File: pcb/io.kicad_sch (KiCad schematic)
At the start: 36 parts, among them J10 Conn_01x02, J2 RJ18, J3 RJ18, J4 Conn_02x05, J5 Conn_01x03, J6 Conn_01x03, J7 Conn_01x02, J8 Conn_01x02, J9 Conn_01x02, Q1 BT148, Q2 BC847, Q3 BC847, U7 6N137, U8 PC817, U9 PC817

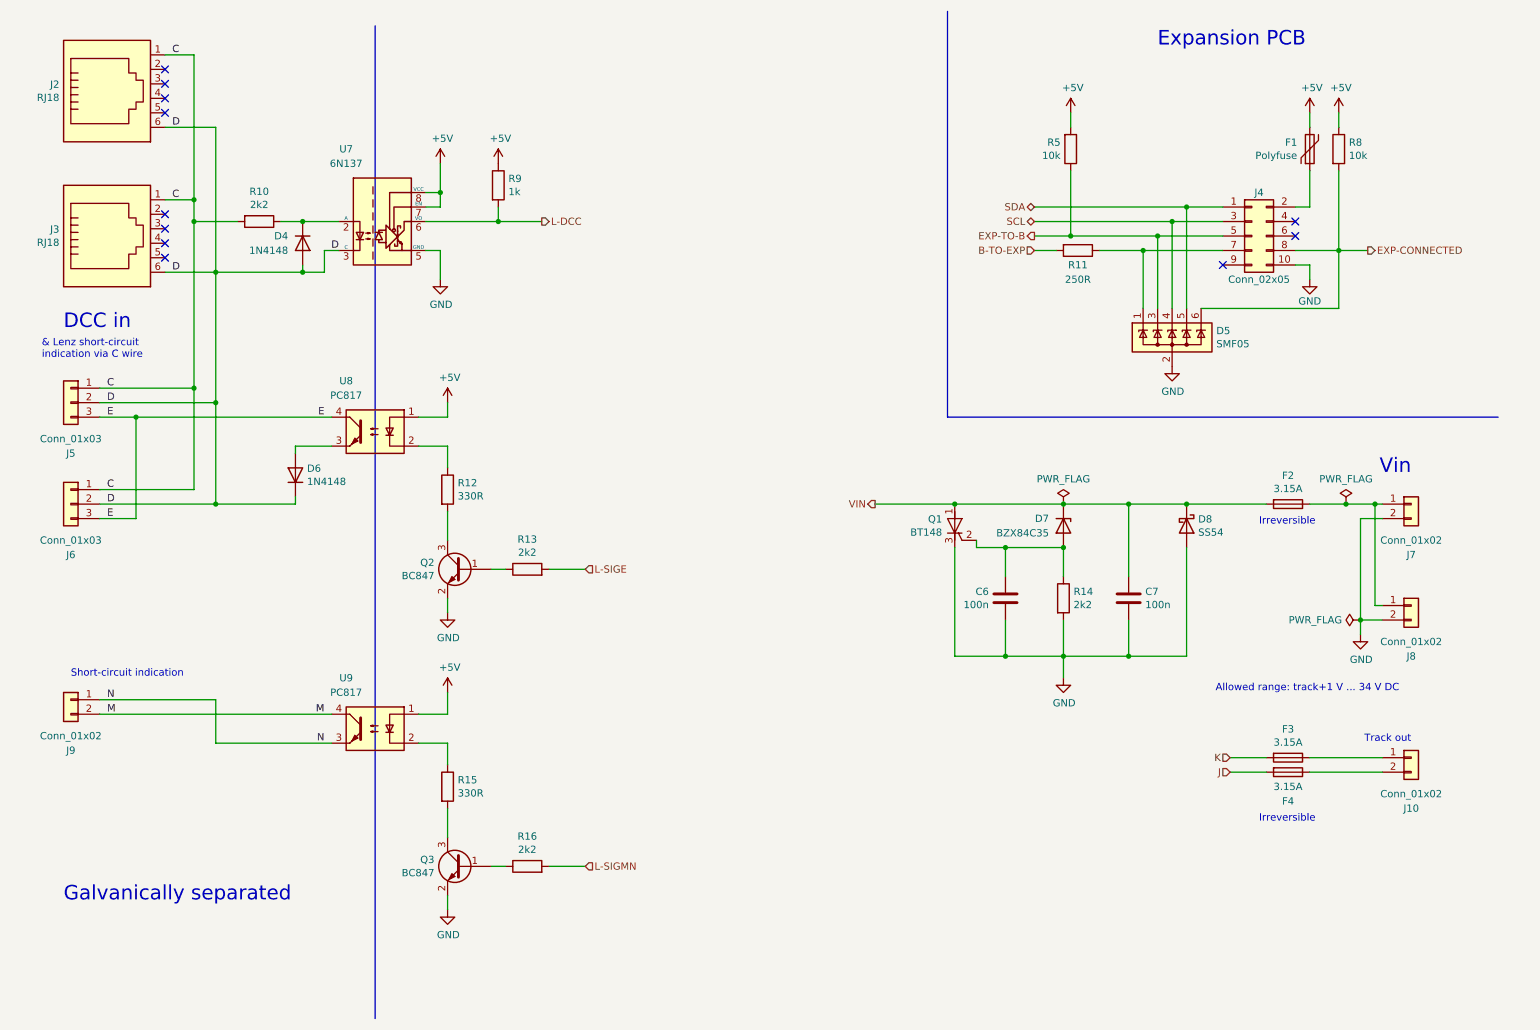
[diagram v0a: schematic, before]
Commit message: Update to KiCad 8.
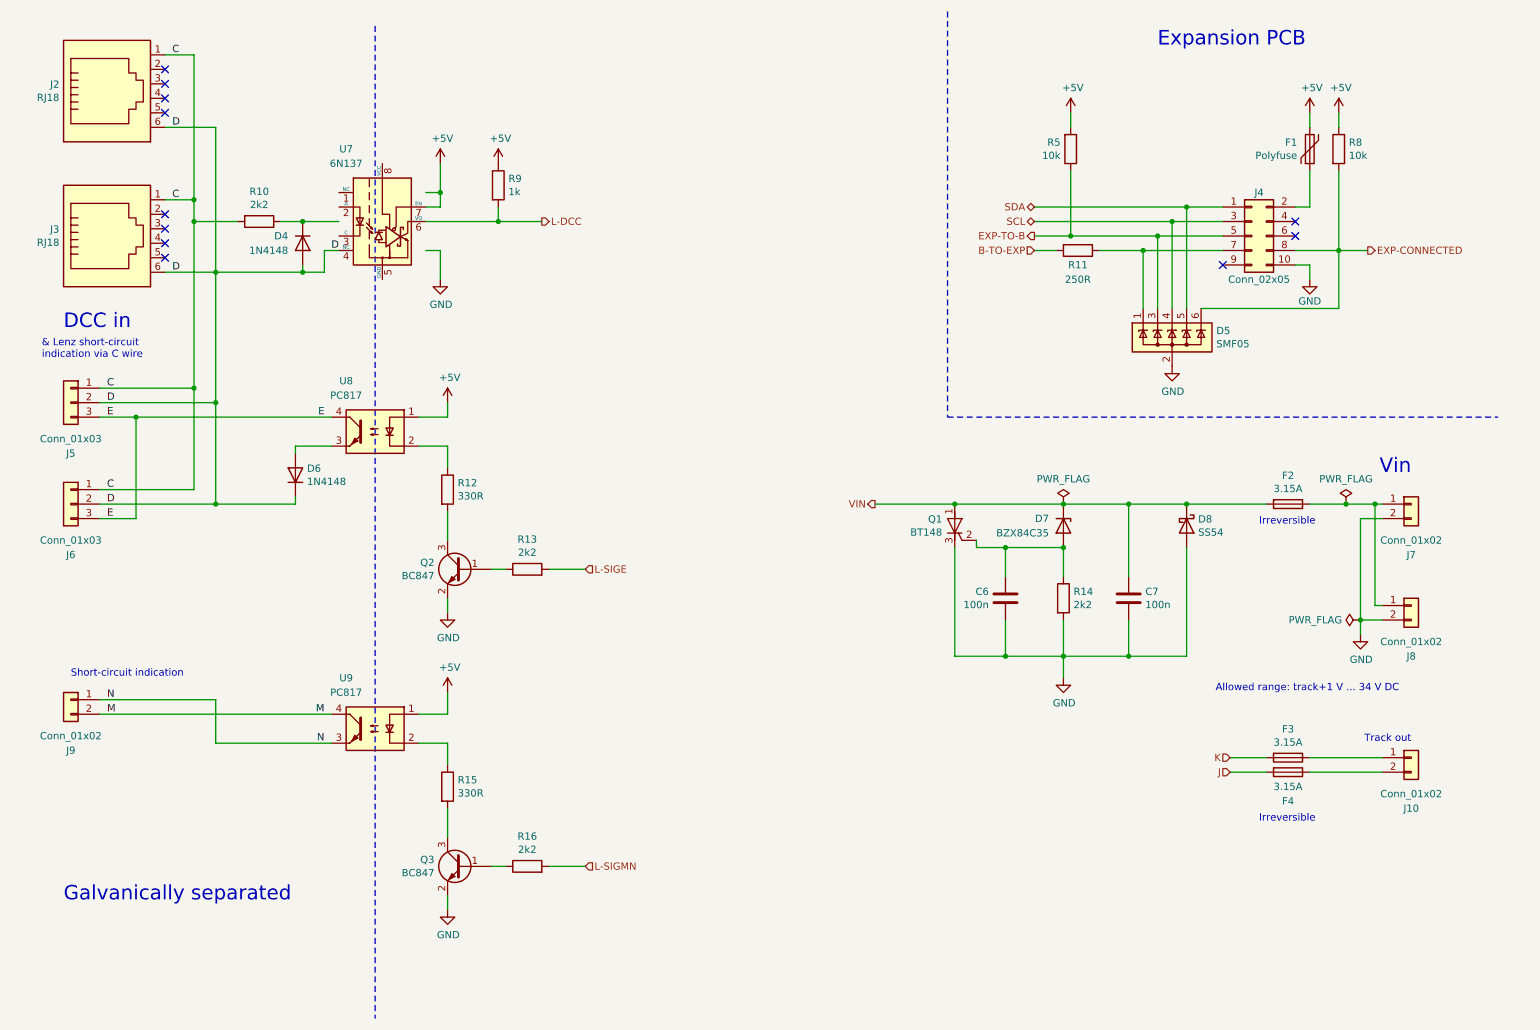
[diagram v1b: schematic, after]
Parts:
- D7: footprint Diode_SMD:D_SOT-23_ANK -> Package_TO_SOT_SMD:SOT-23
- Q1: footprint Package_TO_SOT_SMD:SOT-223 -> Package_TO_SOT_THT:TO-92_Inline
- Q2, Q3: footprint Package_TO_SOT_SMD:SOT-23_Handsoldering -> Package_TO_SOT_SMD:SOT-23
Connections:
- net +5V: no longer U7.8 (VCC)
- net D: now also U7.4 (NC); no longer U7.3 (C)
- net GND: no longer U7.5 (GND)
- net VIN: now also D7.3 (K); no longer D7.1 (K)
- net at D4.1 (K), R10.1: no longer U7.2 (A)
- net at C6.2, Q1.2 (G), R14.1: now also D7.1 (A); no longer D7.2 (A)

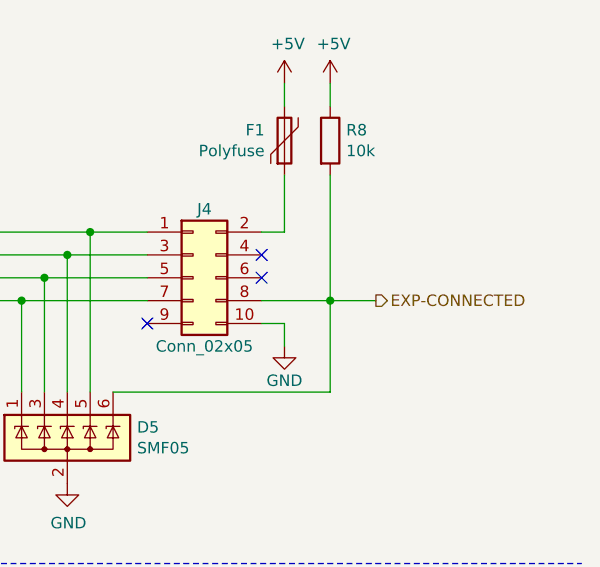
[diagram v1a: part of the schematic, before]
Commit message: Tweak exapander connector.
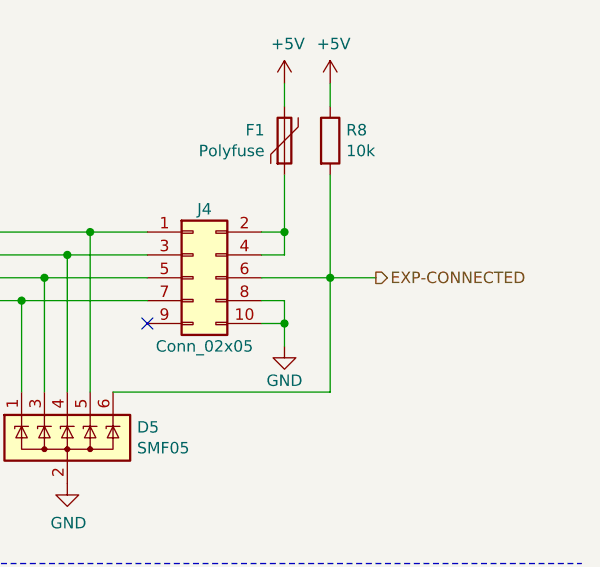
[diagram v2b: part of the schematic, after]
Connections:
- net EXP-CONNECTED: now also J4.6 (Pin_6); no longer J4.8 (Pin_8)
- net GND: now also J4.8 (Pin_8)
- net at F1.1, J4.2 (Pin_2): now also J4.4 (Pin_4)
- no-connect marks 11 -> 9
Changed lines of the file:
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@@
-	)
-	(junction
-		(at 251.46 58.42)
-		(diameter 0)
-		(color 0 0 0 0)
 	)
 	(junction
@@
 	)
 	(junction
+		(at 246.38 50.8)
+		(diameter 0)
+		(color 0 0 0 0)
+	)
+	(junction
 		(at 54.61 102.87)
 		(diameter 0)
@@
 	)
 	(junction
+		(at 246.38 60.96)
+		(diameter 0)
+		(color 0 0 0 0)
+	)
+	(junction
 		(at 193.04 110.49)
 		(diameter 0)
@@
 	(junction
 		(at 219.71 55.88)
+		(diameter 0)
+		(color 0 0 0 0)
+	)
+	(junction
+		(at 251.46 55.88)
 		(diameter 0)
 		(color 0 0 0 0)
@@
 	)
 	(no_connect
-		(at 243.84 53.34)
-	)
-	(no_connect
 		(at 45.72 52.07)
 	)
@@
 	)
 	(no_connect
-		(at 243.84 55.88)
-	)
-	(no_connect
 		(at 45.72 54.61)
 	)
@@
 	(wire
 		(pts
-			(xy 251.46 44.45) (xy 251.46 58.42)
+			(xy 251.46 44.45) (xy 251.46 55.88)
 		)
 		(stroke
@@
 	(wire
 		(pts
+			(xy 243.84 53.34) (xy 246.38 53.34)
+		)
+		(stroke
+			(width 0)
+			(type default)
+		)
+	)
+	(wire
+		(pts
 			(xy 184.15 102.87) (xy 203.2 102.87)
 		)
@@
 	(wire
 		(pts
+			(xy 246.38 50.8) (xy 246.38 53.34)
+		)
+		(stroke
+			(width 0)
+			(type default)
+		)
+	)
+	(wire
+		(pts
 			(xy 68.58 92.71) (xy 74.93 92.71)
 		)
@@
 	(wire
 		(pts
-			(xy 243.84 58.42) (xy 251.46 58.42)
+			(xy 243.84 55.88) (xy 251.46 55.88)
 		)
 		(stroke
@@
 	(wire
 		(pts
+			(xy 246.38 58.42) (xy 246.38 60.96)
+		)
+		(stroke
+			(width 0)
+			(type default)
+		)
+	)
+	(wire
+		(pts
 			(xy 209.55 58.42) (xy 217.17 58.42)
 		)
@@
 	(wire
 		(pts
+			(xy 251.46 55.88) (xy 251.46 68.58)
+		)
+		(stroke
+			(width 0)
+			(type default)
+		)
+	)
+	(wire
+		(pts
 			(xy 201.93 58.42) (xy 198.12 58.42)
 		)
@@
 	(wire
 		(pts
-			(xy 251.46 58.42) (xy 251.46 68.58)
-		)
-		(stroke
-			(width 0)
-			(type default)
-		)
-	)
-	(wire
-		(pts
 			(xy 203.2 110.49) (xy 193.04 110.49)
 		)
@@
 	(wire
 		(pts
-			(xy 251.46 58.42) (xy 256.54 58.42)
+			(xy 251.46 55.88) (xy 256.54 55.88)
 		)
 		(stroke
@@
 		(pts
 			(xy 54.61 36.83) (xy 54.61 62.23)
+		)
+		(stroke
+			(width 0)
+			(type default)
+		)
+	)
+	(wire
+		(pts
+			(xy 243.84 58.42) (xy 246.38 58.42)
 		)
 		(stroke
@@
 	(hierarchical_label "EXP-CONNECTED"
 		(shape output)
-		(at 256.54 58.42 0)
-		(effects
-			(font
+		(at 256.54 55.88 0)
+		(effects
+			(font

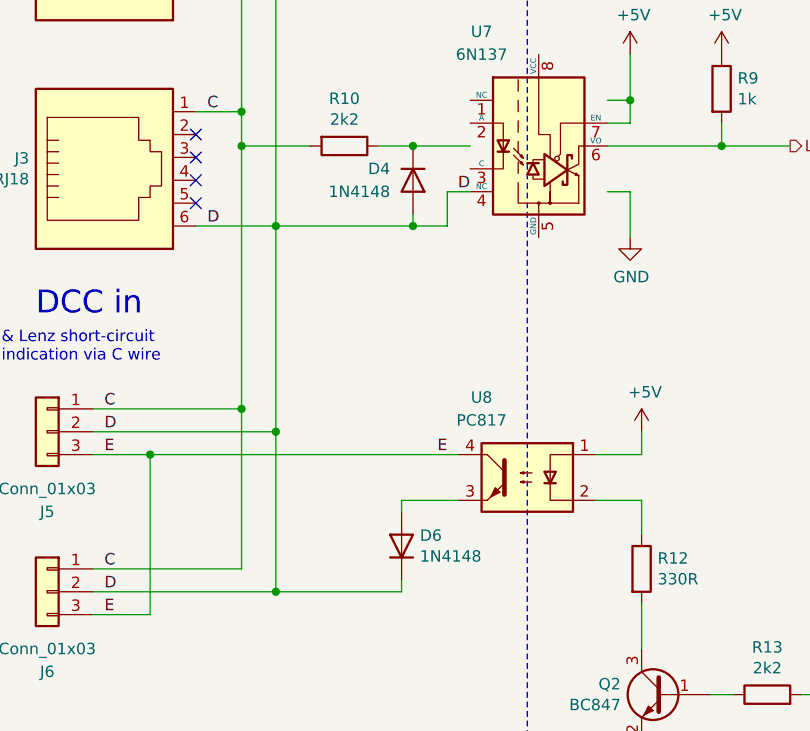
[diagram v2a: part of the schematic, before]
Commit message: Use 1N5819 instead of 1N4148.
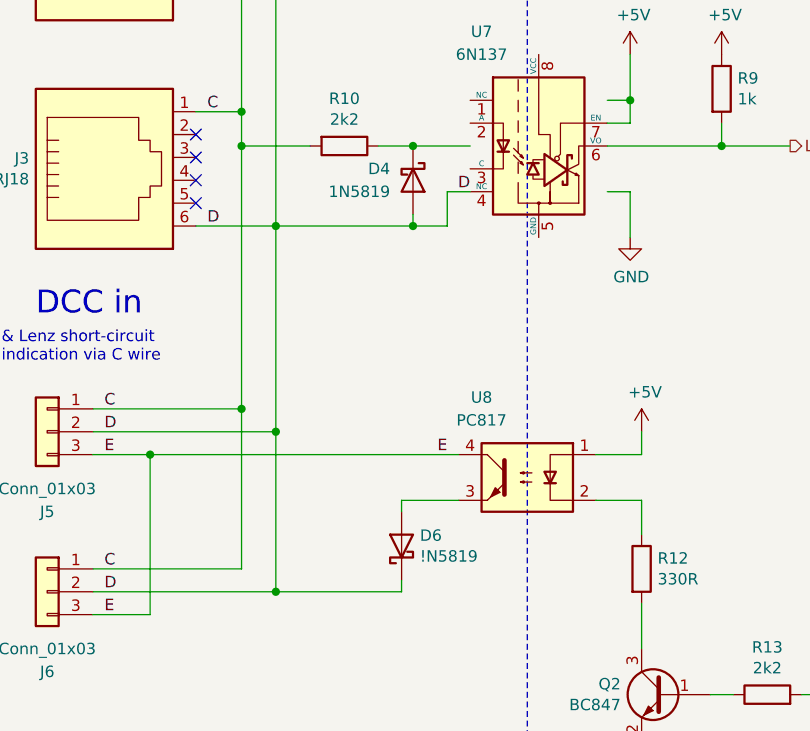
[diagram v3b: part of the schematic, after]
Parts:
- D4: value 1N4148 -> 1N5819; footprint Diode_SMD:D_0805_2012Metric_Pad1.15x1.40mm_HandSolder -> Diode_SMD:D_SOD-123; symbol Device:D -> Device:D_Schottky
- D6: value 1N4148 -> !N5819; footprint Diode_SMD:D_0805_2012Metric_Pad1.15x1.40mm_HandSolder -> Diode_SMD:D_SOD-123; symbol Device:D -> Device:D_Schottky
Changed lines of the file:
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@@
 	)
 	(symbol
-		(lib_id "Device:D")
+		(lib_id "Device:D_Schottky")
 		(at 68.58 97.79 90)
 		(unit 1)
@@
 			)
 		)
-		(property "Value" "1N4148"
+		(property "Value" "!N5819"
 			(at 70.612 98.933 90)
 			(effects
@@
 			)
 		)
-		(property "Footprint" "Diode_SMD:D_0805_2012Metric_Pad1.15x1.40mm_HandSolder"
+		(property "Footprint" "Diode_SMD:D_SOD-123"
 			(at 68.58 97.79 0)
 			(effects
@@
 			)
 		)
-		(property "Description" "Diode"
+		(property "Description" "Schottky diode"
 			(at 68.58 97.79 0)
 			(effects
@@
 	)
 	(symbol
-		(lib_id "Device:D")
+		(lib_id "Device:D_Schottky")
 		(at 69.85 57.15 270)
 		(unit 1)
@@
 			)
 		)
-		(property "Value" "1N4148"
+		(property "Value" "1N5819"
 			(at 67.31 58.42 90)
 			(effects
@@
 			)
 		)
-		(property "Footprint" "Diode_SMD:D_0805_2012Metric_Pad1.15x1.40mm_HandSolder"
+		(property "Footprint" "Diode_SMD:D_SOD-123"
 			(at 69.85 57.15 0)
 			(effects
@@
 			)
 		)
-		(property "Description" "Diode"
+		(property "Description" "Schottky diode"
 			(at 69.85 57.15 0)
 			(effects

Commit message: Export root page escription to other pages.
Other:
- company: (none) -> Model Railroader Club Brno I – KMŽ Brno I – https://kmz-brno.cz/
- title: HB22 – IO -> HB22 – DCC booster
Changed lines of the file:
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@@
 	(paper "A4")
 	(title_block
-		(title "HB22 – IO")
-		(comment 4 "Booster inputs & outputs")
+		(title "HB22 – DCC booster")
+		(date "2025-02-20")
+		(rev "1.0")
+		(company "Model Railroader Club Brno I – KMŽ Brno I – https://kmz-brno.cz/")
+		(comment 1 "Jan Horáček")
+		(comment 2 "https://github.com/kmzbrnoI/hb22")
+		(comment 3 "https://creativecommons.org/licenses/by-sa/4.0/")
+		(comment 4 "Released under the Creative Commons Attribution-ShareAlike 4.0 License")
 	)
 	(junction
